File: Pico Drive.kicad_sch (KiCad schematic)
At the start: 27 parts, among them J1 Conn_01x06_Male, J2 Conn_01x05, J3 Conn_01x03_Male, J4 Conn_01x06, J6 I2C, SW1 Reset, U1 Pico, U2 74AXP1T45GWH, U3 74AHCT1G125DBVTG4

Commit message: Changed all 0402 components to 0805
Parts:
- C1, C2, C3, C4: footprint Capacitor_SMD:C_0402_1005Metric_Pad0.74x0.62mm_HandSolder -> Capacitor_SMD:C_0805_2012Metric_Pad1.18x1.45mm_HandSolder
- D1: footprint LED_SMD:LED_0603_1608Metric_Pad1.05x0.95mm_HandSolder -> LED_SMD:LED_0805_2012Metric_Pad1.15x1.40mm_HandSolder
- R1, R2, R3, R4, R5, R6, R7, R8, R9: footprint Resistor_SMD:R_0402_1005Metric_Pad0.72x0.64mm_HandSolder -> Resistor_SMD:R_0805_2012Metric_Pad1.20x1.40mm_HandSolder
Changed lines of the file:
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@@
       (effects (font (size 1.27 1.27)) (justify left))
     )
-    (property "Footprint" "Capacitor_SMD:C_0402_1005Metric_Pad0.74x0.62mm_HandSolder" (at 42.8752 185.42 0)
+    (property "Footprint" "Capacitor_SMD:C_0805_2012Metric_Pad1.18x1.45mm_HandSolder" (at 42.8752 185.42 0)
       (effects (font (size 1.27 1.27)) hide)
     )
@@
       (effects (font (size 1.27 1.27)) (justify left))
     )
-    (property "Footprint" "Capacitor_SMD:C_0402_1005Metric_Pad0.74x0.62mm_HandSolder" (at 200.3552 115.57 0)
+    (property "Footprint" "Capacitor_SMD:C_0805_2012Metric_Pad1.18x1.45mm_HandSolder" (at 200.3552 115.57 0)
       (effects (font (size 1.27 1.27)) hide)
     )
@@
       (effects (font (size 1.27 1.27)) (justify right))
     )
-    (property "Footprint" "LED_SMD:LED_0603_1608Metric_Pad1.05x0.95mm_HandSolder" (at 22.86 135.89 0)
+    (property "Footprint" "LED_SMD:LED_0805_2012Metric_Pad1.15x1.40mm_HandSolder" (at 22.86 135.89 0)
       (effects (font (size 1.27 1.27)) hide)
     )
@@
       (effects (font (size 1.27 1.27)) (justify left))
     )
-    (property "Footprint" "Resistor_SMD:R_0402_1005Metric_Pad0.72x0.64mm_HandSolder" (at 167.132 111.76 90)
+    (property "Footprint" "Resistor_SMD:R_0805_2012Metric_Pad1.20x1.40mm_HandSolder" (at 167.132 111.76 90)
       (effects (font (size 1.27 1.27)) hide)
     )
@@
       (effects (font (size 1.27 1.27)) (justify left))
     )
-    (property "Footprint" "Resistor_SMD:R_0402_1005Metric_Pad0.72x0.64mm_HandSolder" (at 21.082 126.365 90)
+    (property "Footprint" "Resistor_SMD:R_0805_2012Metric_Pad1.20x1.40mm_HandSolder" (at 21.082 126.365 90)
       (effects (font (size 1.27 1.27)) hide)
     )
@@
       (effects (font (size 1.27 1.27)) (justify left))
     )
-    (property "Footprint" "Capacitor_SMD:C_0402_1005Metric_Pad0.74x0.62mm_HandSolder" (at 162.8902 50.165 0)
+    (property "Footprint" "Capacitor_SMD:C_0805_2012Metric_Pad1.18x1.45mm_HandSolder" (at 162.8902 50.165 0)
       (effects (font (size 1.27 1.27)) hide)
     )
@@
       (effects (font (size 1.27 1.27)) (justify left))
     )
-    (property "Footprint" "Capacitor_SMD:C_0402_1005Metric_Pad0.74x0.62mm_HandSolder" (at 149.5298 50.165 0)
+    (property "Footprint" "Capacitor_SMD:C_0805_2012Metric_Pad1.18x1.45mm_HandSolder" (at 149.5298 50.165 0)
       (effects (font (size 1.27 1.27)) hide)
     )
@@
       (effects (font (size 1.27 1.27)) (justify left))
     )
-    (property "Footprint" "Resistor_SMD:R_0402_1005Metric_Pad0.72x0.64mm_HandSolder" (at 217.932 39.37 90)
+    (property "Footprint" "Resistor_SMD:R_0805_2012Metric_Pad1.20x1.40mm_HandSolder" (at 217.932 39.37 90)
       (effects (font (size 1.27 1.27)) hide)
     )
@@
       (effects (font (size 1.27 1.27)) (justify left))
     )
-    (property "Footprint" "Resistor_SMD:R_0402_1005Metric_Pad0.72x0.64mm_HandSolder" (at 167.132 137.16 90)
+    (property "Footprint" "Resistor_SMD:R_0805_2012Metric_Pad1.20x1.40mm_HandSolder" (at 167.132 137.16 90)
       (effects (font (size 1.27 1.27)) hide)
     )
@@
       (effects (font (size 1.27 1.27)) (justify left))
     )
-    (property "Footprint" "Resistor_SMD:R_0402_1005Metric_Pad0.72x0.64mm_HandSolder" (at 211.582 68.58 90)
+    (property "Footprint" "Resistor_SMD:R_0805_2012Metric_Pad1.20x1.40mm_HandSolder" (at 211.582 68.58 90)
       (effects (font (size 1.27 1.27)) hide)
     )
@@
       (effects (font (size 1.27 1.27)))
     )
-    (property "Footprint" "Resistor_SMD:R_0402_1005Metric_Pad0.72x0.64mm_HandSolder" (at 32.385 176.403 90)
+    (property "Footprint" "Resistor_SMD:R_0805_2012Metric_Pad1.20x1.40mm_HandSolder" (at 32.385 176.403 90)
       (effects (font (size 1.27 1.27)) hide)
     )
@@
       (effects (font (size 1.27 1.27)) (justify left))
     )
-    (property "Footprint" "Resistor_SMD:R_0402_1005Metric_Pad0.72x0.64mm_HandSolder" (at 173.482 68.58 90)
+    (property "Footprint" "Resistor_SMD:R_0805_2012Metric_Pad1.20x1.40mm_HandSolder" (at 173.482 68.58 90)
       (effects (font (size 1.27 1.27)) hide)
     )
@@
       (effects (font (size 1.27 1.27)) (justify left))
     )
-    (property "Footprint" "Resistor_SMD:R_0402_1005Metric_Pad0.72x0.64mm_HandSolder" (at 21.082 167.64 90)
+    (property "Footprint" "Resistor_SMD:R_0805_2012Metric_Pad1.20x1.40mm_HandSolder" (at 21.082 167.64 90)
       (effects (font (size 1.27 1.27)) hide)
     )
@@
       (effects (font (size 1.27 1.27)) (justify left))
     )
-    (property "Footprint" "Resistor_SMD:R_0402_1005Metric_Pad0.72x0.64mm_HandSolder" (at 197.612 137.16 90)
-      (effects (font (size 1.27 1.27)) hide)
-    )
+    (property "Footprint" "Resistor_SMD:R_0805_2012Metric_Pad1.20x1.40mm_HandSolder" (at 197.612 137.16 90)
+      (effects (font (size 1.27 1.27)) hide)
+    )

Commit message: Swapped LED and reset switch, made more space
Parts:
- D1: footprint LED_SMD:LED_0805_2012Metric_Pad1.15x1.40mm_HandSolder -> LED_THT:LED_D3.0mm_Clear
- SW1: footprint digikey-footprints:Switch_Tactile_SMD_4.5x4.5mm_TL3315NF160Q -> Button_Switch_THT:SW_PUSH_6mm_H5mm
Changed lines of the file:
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@@
       (effects (font (size 1.27 1.27)) (justify right))
     )
-    (property "Footprint" "LED_SMD:LED_0805_2012Metric_Pad1.15x1.40mm_HandSolder" (at 22.86 135.89 0)
+    (property "Footprint" "LED_THT:LED_D3.0mm_Clear" (at 22.86 135.89 0)
       (effects (font (size 1.27 1.27)) hide)
     )
@@
       (effects (font (size 1.27 1.27)) (justify right))
     )
-    (property "Footprint" "digikey-footprints:Switch_Tactile_SMD_4.5x4.5mm_TL3315NF160Q" (at 17.78 182.245 0)
-      (effects (font (size 1.27 1.27)) hide)
-    )
+    (property "Footprint" "Button_Switch_THT:SW_PUSH_6mm_H5mm" (at 17.78 182.245 0)
+      (effects (font (size 1.27 1.27)) hide)
+    )

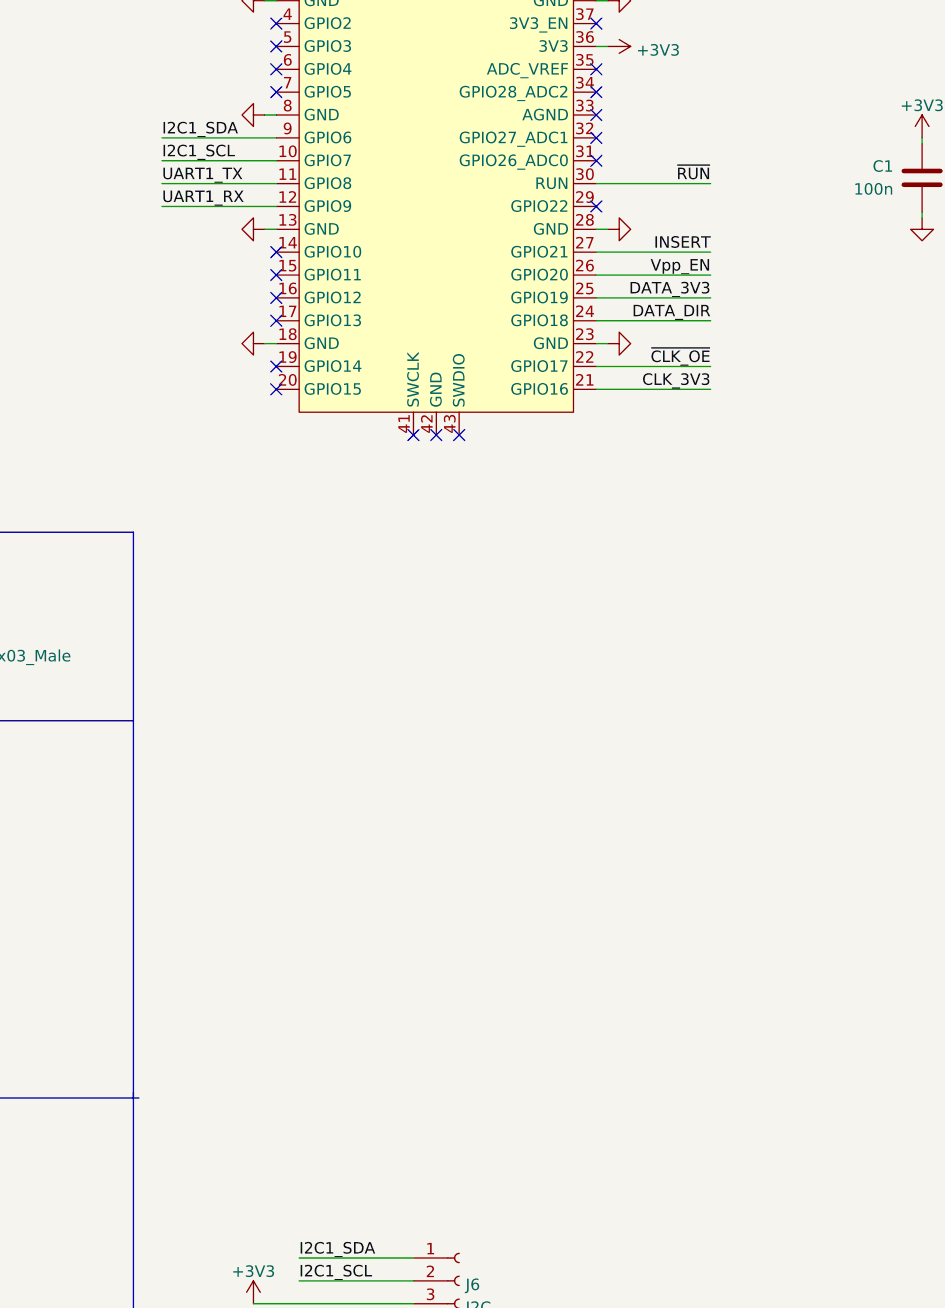
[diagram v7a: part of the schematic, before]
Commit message: Added pullups and decoupling for I2C
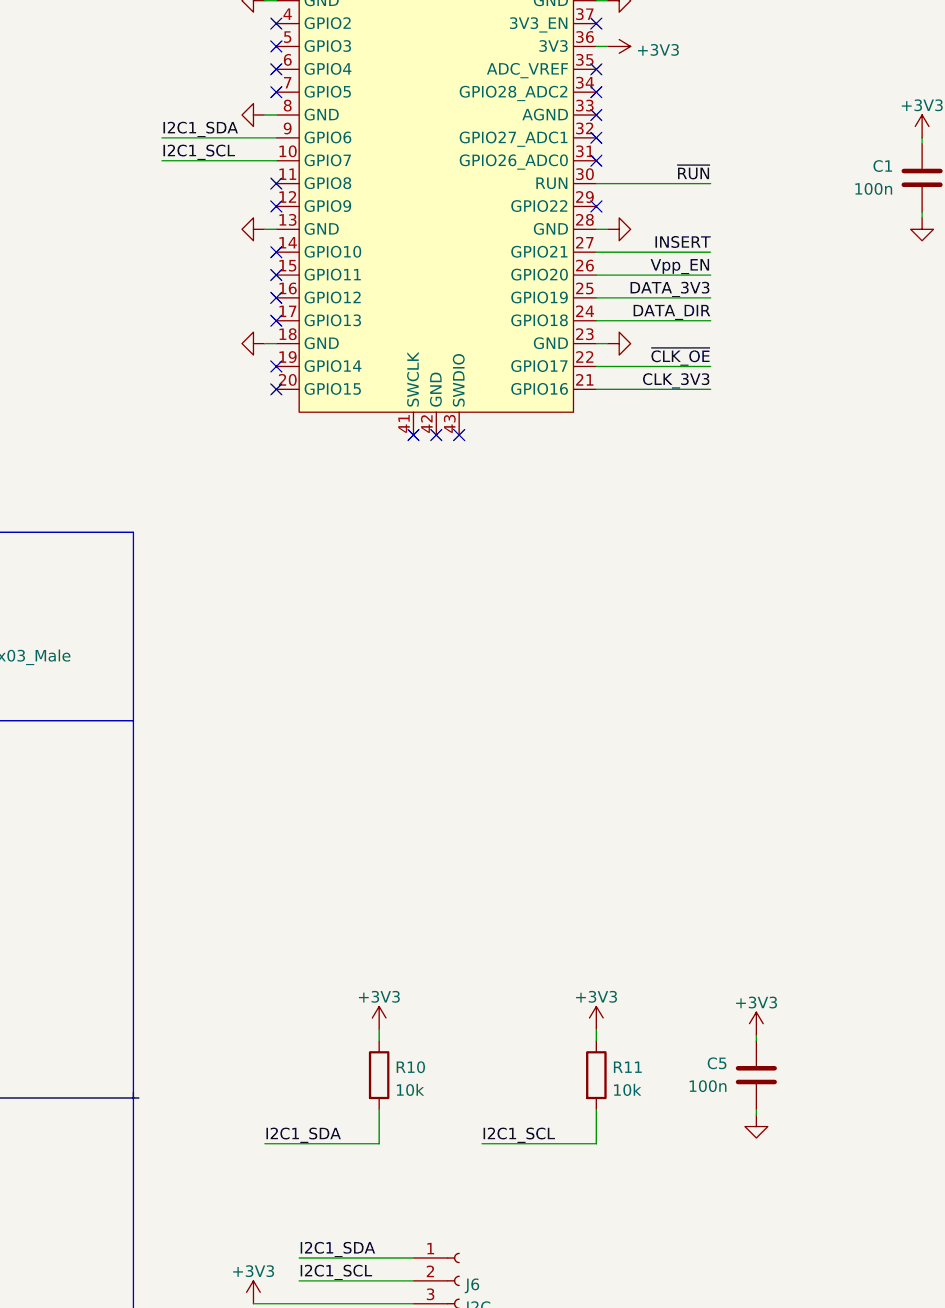
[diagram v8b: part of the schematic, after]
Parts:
- added C5: 100n, Capacitor_SMD:C_0805_2012Metric_Pad1.18x1.45mm_HandSolder, symbol Device:C
- added R10, R11: 10k, Resistor_SMD:R_0805_2012Metric_Pad1.20x1.40mm_HandSolder, symbol Device:R
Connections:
- net +3V3: now also C5.1, R10.1, R11.1
- net GND: now also C5.2
- net I2C1_SCL: now also R11.2
- net I2C1_SDA: now also R10.2
- net UART1_RX: no longer names the net of U1.12 (GPIO9)
- net UART1_TX: no longer names the net of U1.11 (GPIO8)
- no-connect marks 21 -> 23
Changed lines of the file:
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@@
   )
   (no_connect (at 78.74 31.75))
+  (no_connect (at 78.74 46.99))
   (no_connect (at 78.74 69.85))
   (no_connect (at 114.3 24.13))
@@
   (no_connect (at 114.3 36.83))
   (no_connect (at 78.74 62.23))
+  (no_connect (at 78.74 49.53))
   (no_connect (at 78.74 36.83))
   (no_connect (at 78.74 59.69))
@@
     (stroke (width 0) (type default))
   )
-  (wire (pts (xy 66.04 49.53) (xy 78.74 49.53))
-    (stroke (width 0) (type default))
-  )
   (wire (pts (xy 168.91 119.38) (xy 187.96 119.38))
     (stroke (width 0) (type default))
@@
     (stroke (width 0) (type default))
   )
+  (wire (pts (xy 77.47 153.67) (xy 90.17 153.67))
+    (stroke (width 0) (type default))
+  )
+  (wire (pts (xy 132.08 150.495) (xy 132.08 149.86))
+    (stroke (width 0) (type default))
+  )
   (wire (pts (xy 199.39 130.81) (xy 215.9 130.81))
     (stroke (width 0) (type default))
   )
-  (wire (pts (xy 66.04 46.99) (xy 78.74 46.99))
-    (stroke (width 0) (type default))
-  )
   (wire (pts (xy 127 54.61) (xy 114.3 54.61))
     (stroke (width 0) (type default))
@@
     (stroke (width 0) (type default))
   )
+  (wire (pts (xy 90.17 153.67) (xy 90.17 149.86))
+    (stroke (width 0) (type default))
+  )
   (polyline (pts (xy 62.865 106.68) (xy 62.865 148.59))
     (stroke (width 0) (type default))
@@
     (stroke (width 0) (type default))
   )
+  (wire (pts (xy 90.17 140.97) (xy 90.17 142.24))
+    (stroke (width 0) (type default))
+  )
   (wire (pts (xy 232.41 139.7) (xy 232.41 140.97))
     (stroke (width 0) (type default))
@@
     (stroke (width 0) (type default))
   )
+  (wire (pts (xy 114.3 140.97) (xy 114.3 142.24))
+    (stroke (width 0) (type default))
+  )
   (polyline (pts (xy 12.7 148.59) (xy 63.5 148.59))
     (stroke (width 0) (type default))
@@
     (stroke (width 0) (type default))
   )
+  (wire (pts (xy 101.6 153.67) (xy 114.3 153.67))
+    (stroke (width 0) (type default))
+  )
   (wire (pts (xy 76.2 173.99) (xy 93.98 173.99))
     (stroke (width 0) (type default))
   )
+  (wire (pts (xy 132.08 141.605) (xy 132.08 142.24))
+    (stroke (width 0) (type default))
+  )
   (wire (pts (xy 194.31 130.81) (xy 199.39 130.81))
     (stroke (width 0) (type default))
@@
   )
   (wire (pts (xy 41.91 174.625) (xy 41.91 177.8))
+    (stroke (width 0) (type default))
+  )
+  (wire (pts (xy 114.3 153.67) (xy 114.3 149.86))
     (stroke (width 0) (type default))
   )
@@
     (effects (font (size 1.27 1.27)) (justify left bottom))
   )
+  (label "I2C1_SDA" (at 77.47 153.67 0) (fields_autoplaced)
+    (effects (font (size 1.27 1.27)) (justify left bottom))
+  )
   (label "I2C1_SDA" (at 66.04 41.91 0) (fields_autoplaced)
     (effects (font (size 1.27 1.27)) (justify left bottom))
@@
     (effects (font (size 1.27 1.27)) (justify left bottom))
   )
-  (label "UART1_RX" (at 66.04 49.53 0) (fields_autoplaced)
-    (effects (font (size 1.27 1.27)) (justify left bottom))
-  )
   (label "~{CLK_OE}" (at 242.57 115.57 0) (fields_autoplaced)
     (effects (font (size 1.27 1.27)) (justify left bottom))
@@
     (effects (font (size 1.27 1.27)) (justify left bottom))
   )
+  (label "I2C1_SCL" (at 101.6 153.67 0) (fields_autoplaced)
+    (effects (font (size 1.27 1.27)) (justify left bottom))
+  )
   (label "UART0_RX" (at 66.04 24.13 0) (fields_autoplaced)
     (effects (font (size 1.27 1.27)) (justify left bottom))
@@
   (label "~{RUN}" (at 127 46.99 180) (fields_autoplaced)
     (effects (font (size 1.27 1.27)) (justify right bottom))
-  )
-  (label "UART1_TX" (at 66.04 46.99 0) (fields_autoplaced)
-    (effects (font (size 1.27 1.27)) (justify left bottom))
   )
   (label "UART0_TX" (at 66.04 21.59 0) (fields_autoplaced)
@@
     )
   )
+  (symbol (lib_id "Device:C") (at 132.08 146.05 0) (mirror y) (unit 1)
+    (in_bom yes) (on_board yes) (dnp no)
+    (property "Reference" "C5" (at 128.905 144.78 0)
+      (effects (font (size 1.27 1.27)) (justify left))
+    )
+    (property "Value" "100n" (at 128.905 147.32 0)
+      (effects (font (size 1.27 1.27)) (justify left))
+    )
+    (property "Footprint" "Capacitor_SMD:C_0805_2012Metric_Pad1.18x1.45mm_HandSolder" (at 131.1148 149.86 0)
+      (effects (font (size 1.27 1.27)) hide)
+    )
+    (property "Datasheet" "~" (at 132.08 146.05 0)
+      (effects (font (size 1.27 1.27)) hide)
+    )
+    (pin "1")
+    (pin "2")
+    (instances
+      (project "Pico Drive"
+        (path "/f0c645b2-2abc-48f6-92b5-6f27f706b833"
+          (reference "C5") (unit 1)
+        )
+      )
+    )
+  )
   (symbol (lib_id "power:GND") (at 180.34 57.15 0) (unit 1)
     (in_bom yes) (on_board yes) (dnp no)
@@
         (path "/f0c645b2-2abc-48f6-92b5-6f27f706b833"
           (reference "#PWR0103") (unit 1)
+        )
+      )
+    )
+  )
+  (symbol (lib_id "power:+3V3") (at 114.3 140.97 0) (unit 1)
+    (in_bom yes) (on_board yes) (dnp no) (fields_autoplaced)
+    (property "Reference" "#PWR04" (at 114.3 144.78 0)
+      (effects (font (size 1.27 1.27)) hide)
+    )
+    (property "Value" "+3V3" (at 114.3 137.3942 0)
+      (effects (font (size 1.27 1.27)))
+    )
+    (property "Footprint" "" (at 114.3 140.97 0)
+      (effects (font (size 1.27 1.27)) hide)
+    )
+    (property "Datasheet" "" (at 114.3 140.97 0)
+      (effects (font (size 1.27 1.27)) hide)
+    )
+    (pin "1")
+    (instances
+      (project "Pico Drive"
+        (path "/f0c645b2-2abc-48f6-92b5-6f27f706b833"
+          (reference "#PWR04") (unit 1)
         )
       )
@@
     )
   )
+  (symbol (lib_id "power:+3V3") (at 132.08 141.605 0) (unit 1)
+    (in_bom yes) (on_board yes) (dnp no) (fields_autoplaced)
+    (property "Reference" "#PWR05" (at 132.08 145.415 0)
+      (effects (font (size 1.27 1.27)) hide)
+    )
+    (property "Value" "+3V3" (at 132.08 138.0292 0)
+      (effects (font (size 1.27 1.27)))
+    )
+    (property "Footprint" "" (at 132.08 141.605 0)
+      (effects (font (size 1.27 1.27)) hide)
+    )
+    (property "Datasheet" "" (at 132.08 141.605 0)
+      (effects (font (size 1.27 1.27)) hide)
+    )
+    (pin "1")
+    (instances
+      (project "Pico Drive"
+        (path "/f0c645b2-2abc-48f6-92b5-6f27f706b833"
+          (reference "#PWR05") (unit 1)
+        )
+      )
+    )
+  )
   (symbol (lib_id "Mechanical:MountingHole") (at 264.16 17.78 0) (unit 1)
     (in_bom yes) (on_board yes) (dnp no) (fields_autoplaced)
@@
     )
   )
+  (symbol (lib_id "Device:R") (at 90.17 146.05 0) (unit 1)
+    (in_bom yes) (on_board yes) (dnp no) (fields_autoplaced)
+    (property "Reference" "R10" (at 91.948 145.2153 0)
+      (effects (font (size 1.27 1.27)) (justify left))
+    )
+    (property "Value" "10k" (at 91.948 147.7522 0)
+      (effects (font (size 1.27 1.27)) (justify left))
+    )
+    (property "Footprint" "Resistor_SMD:R_0805_2012Metric_Pad1.20x1.40mm_HandSolder" (at 88.392 146.05 90)
+      (effects (font (size 1.27 1.27)) hide)
+    )
+    (property "Datasheet" "~" (at 90.17 146.05 0)
+      (effects (font (size 1.27 1.27)) hide)
+    )
+    (pin "1")
+    (pin "2")
+    (instances
+      (project "Pico Drive"
+        (path "/f0c645b2-2abc-48f6-92b5-6f27f706b833"
+          (reference "R10") (unit 1)
+        )
+      )
+    )
+  )
   (symbol (lib_id "Device:R") (at 213.36 68.58 0) (unit 1)
     (in_bom yes) (on_board yes) (dnp no)
@@
     )
   )
+  (symbol (lib_id "Device:R") (at 114.3 146.05 0) (unit 1)
+    (in_bom yes) (on_board yes) (dnp no) (fields_autoplaced)
+    (property "Reference" "R11" (at 116.078 145.2153 0)
+      (effects (font (size 1.27 1.27)) (justify left))
+    )
+    (property "Value" "10k" (at 116.078 147.7522 0)
+      (effects (font (size 1.27 1.27)) (justify left))
+    )
+    (property "Footprint" "Resistor_SMD:R_0805_2012Metric_Pad1.20x1.40mm_HandSolder" (at 112.522 146.05 90)
+      (effects (font (size 1.27 1.27)) hide)
+    )
+    (property "Datasheet" "~" (at 114.3 146.05 0)
+      (effects (font (size 1.27 1.27)) hide)
+    )
+    (pin "1")
+    (pin "2")
+    (instances
+      (project "Pico Drive"
+        (path "/f0c645b2-2abc-48f6-92b5-6f27f706b833"
+          (reference "R11") (unit 1)
+        )
+      )
+    )
+  )
   (symbol (lib_id "power:GND") (at 189.23 132.08 0) (unit 1)
     (in_bom yes) (on_board yes) (dnp no)
@@
         (path "/f0c645b2-2abc-48f6-92b5-6f27f706b833"
           (reference "#PWR0121") (unit 1)
+        )
+      )
+    )
+  )
+  (symbol (lib_id "power:+3V3") (at 90.17 140.97 0) (unit 1)
+    (in_bom yes) (on_board yes) (dnp no) (fields_autoplaced)
+    (property "Reference" "#PWR03" (at 90.17 144.78 0)
+      (effects (font (size 1.27 1.27)) hide)
+    )
+    (property "Value" "+3V3" (at 90.17 137.3942 0)
+      (effects (font (size 1.27 1.27)))
+    )
+    (property "Footprint" "" (at 90.17 140.97 0)
+      (effects (font (size 1.27 1.27)) hide)
+    )
+    (property "Datasheet" "" (at 90.17 140.97 0)
+      (effects (font (size 1.27 1.27)) hide)
+    )
+    (pin "1")
+    (instances
+      (project "Pico Drive"
+        (path "/f0c645b2-2abc-48f6-92b5-6f27f706b833"
+          (reference "#PWR03") (unit 1)
         )
       )
@@
         )
       )
+    )
+  )
+  (symbol (lib_id "power:GND") (at 132.08 150.495 0) (unit 1)
+    (in_bom yes) (on_board yes) (dnp no)
+    (property "Reference" "#PWR06" (at 132.08 156.845 0)
+      (effects (font (size 1.27 1.27)) hide)
+    )
+    (property "Value" "GND" (at 129.54 153.035 0)
+      (effects (font (size 1.27 1.27)) hide)
+    )
+    (property "Footprint" "" (at 132.08 150.495 0)
+      (effects (font (size 1.27 1.27)) hide)
+    )
+    (property "Datasheet" "" (at 132.08 150.495 0)
+      (effects (font (size 1.27 1.27)) hide)
+    )
+    (pin "1")
+    (instances
+      (project "Pico Drive"
+        (path "/f0c645b2-2abc-48f6-92b5-6f27f706b833"
+          (reference "#PWR06") (unit 1)
+        )
+      )
